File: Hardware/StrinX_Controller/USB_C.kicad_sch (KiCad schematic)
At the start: 6 parts, among them J2 USB_C_16p

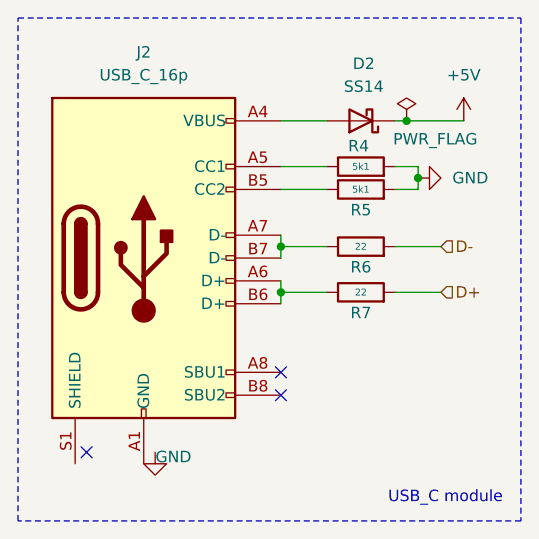
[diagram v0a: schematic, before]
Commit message: Add device and footprint
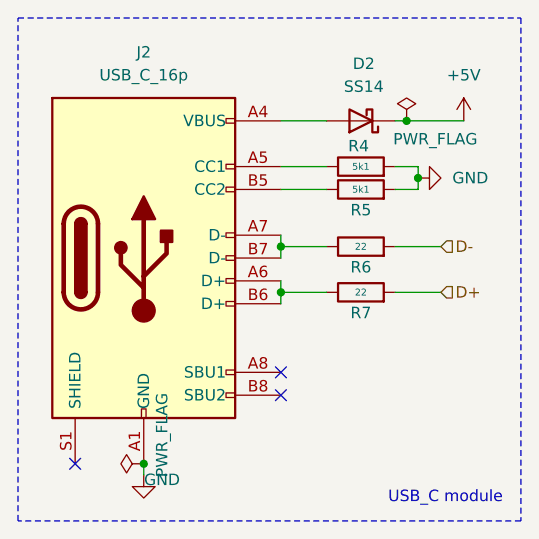
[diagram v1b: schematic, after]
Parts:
- J2: footprint (none) -> Connector_USB:USB_C_Receptacle_HRO_TYPE-C-31-M-12
- R4, R5, R6, R7: footprint (none) -> Resistor_SMD:R_0603_1608Metric
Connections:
- net GND: now also J2.A1 (GND), J2.A12 (GND), J2.B1 (GND), J2.B12 (GND)
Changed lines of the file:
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@@
+	)
+	(junction
+		(at 57.15 115.57)
+		(diameter 0)
+		(color 0 0 0 0)
 	)
 	(junction
@@
 	)
 	(no_connect
-		(at 50.8 114.3)
+		(at 49.53 115.57)
 	)
 	(wire
@@
 		(pts
 			(xy 85.09 96.52) (xy 90.17 96.52)
+		)
+		(stroke
+			(width 0)
+			(type default)
+		)
+	)
+	(wire
+		(pts
+			(xy 57.15 116.84) (xy 57.15 115.57)
 		)
 		(stroke
@@
 		(on_board yes)
 		(dnp no)
-		(property "Reference" "#FLG?"
+		(property "Reference" "#FLG01"
 			(at 86.36 75.565 0)
 			(effects
@@
 			(project ""
 				(path "/60efaa1b-44bb-4814-90d0-8b9990f45080"
+					(reference "#FLG?")
+					(unit 1)
+				)
+				(path "/60efaa1b-44bb-4814-90d0-8b9990f45080/096688d9-d10c-46a8-add9-a537cdfbf42d"
 					(reference "#FLG01")
-					(unit 1)
-				)
-				(path "/60efaa1b-44bb-4814-90d0-8b9990f45080/096688d9-d10c-46a8-add9-a537cdfbf42d"
-					(reference "#FLG?")
 					(unit 1)
 				)
@@
 			)
 		)
-		(property "Footprint" ""
+		(property "Footprint" "Resistor_SMD:R_0603_1608Metric"
 			(at 81.28 93.218 90)
 			(effects
@@
 		(dnp no)
 		(fields_autoplaced yes)
-		(property "Reference" "#PWR?"
+		(property "Reference" "#PWR021"
 			(at 93.98 83.82 0)
 			(effects
@@
 			(project ""
 				(path "/60efaa1b-44bb-4814-90d0-8b9990f45080"
-					(reference "#PWR02")
-					(unit 1)
-				)
-				(path "/60efaa1b-44bb-4814-90d0-8b9990f45080/096688d9-d10c-46a8-add9-a537cdfbf42d"
 					(reference "#PWR?")
 					(unit 1)
 				)
+				(path "/60efaa1b-44bb-4814-90d0-8b9990f45080/096688d9-d10c-46a8-add9-a537cdfbf42d"
+					(reference "#PWR021")
+					(unit 1)
+				)
 			)
 		)
@@
 	(symbol
 		(lib_id "power:GND")
-		(at 58.42 114.3 0)
-		(unit 1)
-		(exclude_from_sim no)
-		(in_bom yes)
-		(on_board yes)
-		(dnp no)
-		(property "Reference" "#PWR?"
-			(at 58.42 120.65 0)
+		(at 57.15 116.84 0)
+		(unit 1)
+		(exclude_from_sim no)
+		(in_bom yes)
+		(on_board yes)
+		(dnp no)
+		(property "Reference" "#PWR022"
+			(at 57.15 123.19 0)
 			(effects
 				(font
@@
 		)
 		(property "Value" "GND"
-			(at 60.452 114.808 0)
+			(at 59.182 117.348 0)
 			(effects
 				(font
@@
 		)
 		(property "Footprint" ""
-			(at 58.42 114.3 0)
+			(at 57.15 116.84 0)
 			(effects
 				(font
@@
 		)
 		(property "Datasheet" ""
-			(at 58.42 114.3 0)
+			(at 57.15 116.84 0)
 			(effects
 				(font
@@
 		)
 		(property "Description" "Power symbol creates a global label with name \"GND\" , ground"
-			(at 58.42 114.3 0)
+			(at 57.15 116.84 0)
 			(effects
 				(font
@@
 			(project ""
 				(path "/60efaa1b-44bb-4814-90d0-8b9990f45080"
-					(reference "#PWR03")
-					(unit 1)
-				)
-				(path "/60efaa1b-44bb-4814-90d0-8b9990f45080/096688d9-d10c-46a8-add9-a537cdfbf42d"
 					(reference "#PWR?")
+					(unit 1)
+				)
+				(path "/60efaa1b-44bb-4814-90d0-8b9990f45080/096688d9-d10c-46a8-add9-a537cdfbf42d"
+					(reference "#PWR022")
 					(unit 1)
 				)
@@
 			)
 		)
-		(property "Footprint" ""
+		(property "Footprint" "Resistor_SMD:R_0603_1608Metric"
 			(at 81.28 84.328 90)
 			(effects
@@
 				(path "/60efaa1b-44bb-4814-90d0-8b9990f45080/096688d9-d10c-46a8-add9-a537cdfbf42d"
 					(reference "R4")
+					(unit 1)
+				)
+			)
+		)
+	)
+	(symbol
+		(lib_id "power:PWR_FLAG")
+		(at 57.15 115.57 90)
+		(mirror x)
+		(unit 1)
+		(exclude_from_sim no)
+		(in_bom yes)
+		(on_board yes)
+		(dnp no)
+		(property "Reference" "#FLG02"
+			(at 55.245 115.57 0)
+			(effects
+				(font
+					(size 1.27 1.27)
+				)
+				(hide yes)
+			)
+		)
+		(property "Value" "PWR_FLAG"
+			(at 59.182 107.696 0)
+			(effects
+				(font
+					(size 1.27 1.27)
+				)
+				(justify left)
+			)
+		)
+		(property "Footprint" ""
+			(at 57.15 115.57 0)
+			(effects
+				(font
+					(size 1.27 1.27)
+				)
+				(hide yes)
+			)
+		)
+		(property "Datasheet" "~"
+			(at 57.15 115.57 0)
+			(effects
+				(font
+					(size 1.27 1.27)
+				)
+				(hide yes)
+			)
+		)
+		(property "Description" "Special symbol for telling ERC where power comes from"
+			(at 57.15 115.57 0)
+			(effects
+				(font
+					(size 1.27 1.27)
+				)
+				(hide yes)
+			)
+		)
+		(pin "1"
+		)
+		(instances
+			(project "StrinX_Controller"
+				(path "/60efaa1b-44bb-4814-90d0-8b9990f45080/096688d9-d10c-46a8-add9-a537cdfbf42d"
+					(reference "#FLG02")
 					(unit 1)
 				)
@@
 			)
 		)
-		(property "Footprint" ""
+		(property "Footprint" "Connector_USB:USB_C_Receptacle_HRO_TYPE-C-31-M-12"
 			(at 60.96 92.71 0)
 			(effects
@@
 			(project ""
 				(path "/60efaa1b-44bb-4814-90d0-8b9990f45080"
-					(reference "J1")
+					(reference "J?")
 					(unit 1)
 				)
@@
 			(project ""
 				(path "/60efaa1b-44bb-4814-90d0-8b9990f45080"
-					(reference "D1")
+					(reference "D?")
 					(unit 1)
 				)
@@
 			)
 		)
-		(property "Footprint" ""
+		(property "Footprint" "Resistor_SMD:R_0603_1608Metric"
 			(at 81.28 98.298 90)
 			(effects
@@
 			)
 		)
-		(property "Footprint" ""
+		(property "Footprint" "Resistor_SMD:R_0603_1608Metric"
 			(at 81.28 86.868 90)
 			(effects
@@
 			(project ""
 				(path "/60efaa1b-44bb-4814-90d0-8b9990f45080"
-					(reference "R1")
+					(reference "R?")
 					(unit 1)
 				)
@@
 		(dnp no)
 		(fields_autoplaced yes)
-		(property "Reference" "#PWR?"
+		(property "Reference" "#PWR020"
 			(at 92.71 81.28 0)
 			(effects
@@
 			(project ""
 				(path "/60efaa1b-44bb-4814-90d0-8b9990f45080"
-					(reference "#PWR01")
-					(unit 1)
-				)
-				(path "/60efaa1b-44bb-4814-90d0-8b9990f45080/096688d9-d10c-46a8-add9-a537cdfbf42d"
 					(reference "#PWR?")
 					(unit 1)
 				)
+				(path "/60efaa1b-44bb-4814-90d0-8b9990f45080/096688d9-d10c-46a8-add9-a537cdfbf42d"
+					(reference "#PWR020")
+					(unit 1)
+				)
